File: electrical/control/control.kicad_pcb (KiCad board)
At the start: 2 copper layers, 33 x 48 mm, 42 parts, among them J1 USB4105-GF-A, J2 SWD, J3 TC2030-NL, J4 UART, J5 QWIIC, SW1 228EMSARGFR, U1 USBLC6-2P6, U2 LP5912-3.3DRV, U3 W25Q16JVUXIQ, U4 RP2040, U5 ABPMRRV060MG2A3, Y1 ABM8-272-T3

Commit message: More PCB tweaks
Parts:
- moved J5 2.41 mm to (166.5, 109.1)
- moved C18 2.41 mm to (161.0, 107.9)
- moved U5 2.41 mm to (154.0, 108.4)
- moved J3 2.15 mm to (166.4, 102.0)
- moved C10 2.00 mm to (153.4, 86.0)
- moved C11 2.00 mm to (155.0, 98.6)
- moved C12 2.00 mm to (152.4, 85.6)
- moved C13 2.00 mm to (157.6, 87.0)
- moved C14 2.00 mm to (156.6, 86.1)
- moved C15 2.00 mm to (147.6, 84.0)
- moved C16 2.00 mm to (152.0, 98.2)
- moved C17 2.00 mm to (152.0, 100.2)
- moved C4 2.00 mm to (148.6, 88.8)
- moved C5 2.00 mm to (148.6, 93.2)
- moved C6 2.00 mm to (154.0, 98.6)
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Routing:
- net RUN: track 26.7 -> 18.2 mm
- net I2C_SCL: track 38.4 -> 37.0 mm
- net SWDIO: track 20.7 -> 19.5 mm
- net Net-(U4-GPIO25): track 26.3 -> 25.2 mm
- net Net-(R8-Pad2): track 25.9 -> 24.7 mm
- net USB_D-: track 6.22 -> 7.37 mm
- net Net-(U4-GPIO26_ADC0): track 22.8 -> 21.6 mm
- net USB_D+: track 6.22 -> 7.37 mm
- net I2C_SDA: track 46.1 -> 45.2 mm
- net SWCLK: track 19.0 -> 18.2 mm
- net PRESSURE_INT: track 32.8 -> 32.0 mm
- net UART_TX: track 25.2 -> 24.6 mm
- net GND: track 62.5 -> 63.0 mm, vias 33 -> 32
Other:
- board size 33 x 48 mm -> 32 x 46 mm
- board text added: "BBMI MIDI Concertina Controller Rev 1"

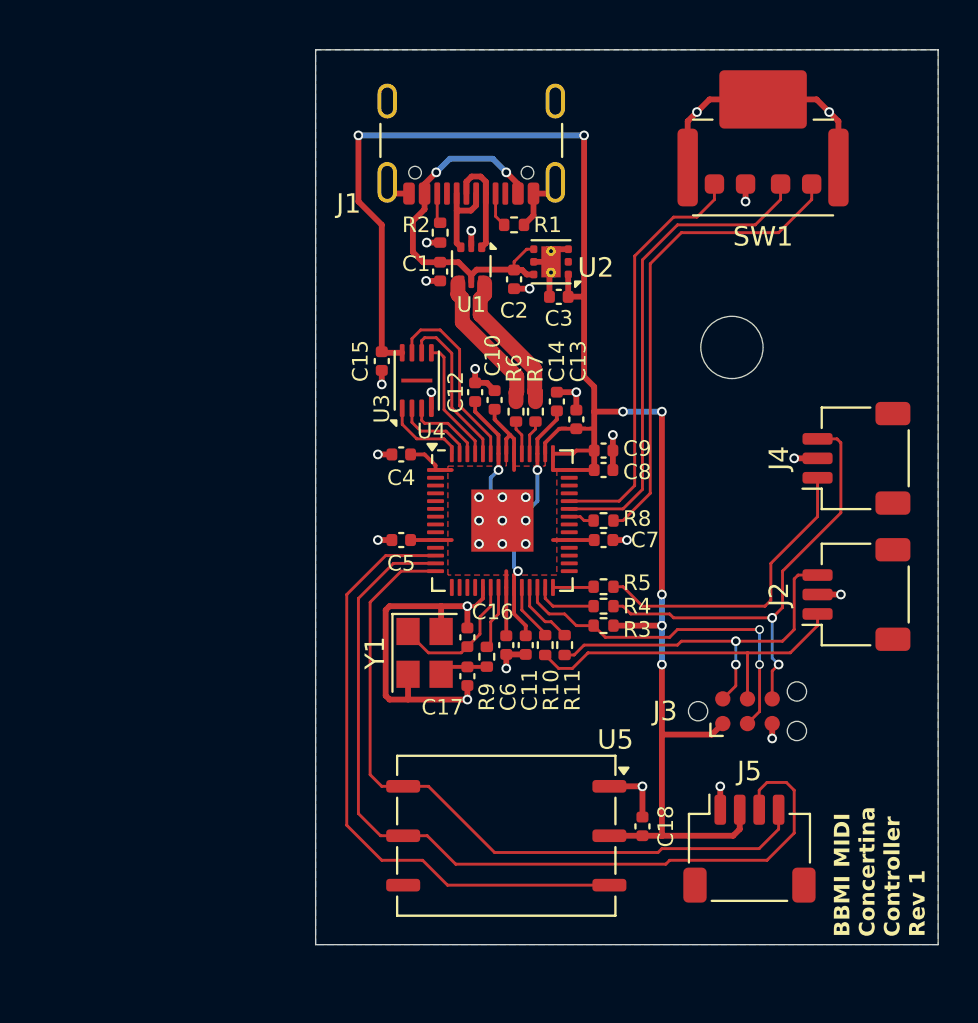
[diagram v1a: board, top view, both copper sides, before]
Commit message: Position mechanical components
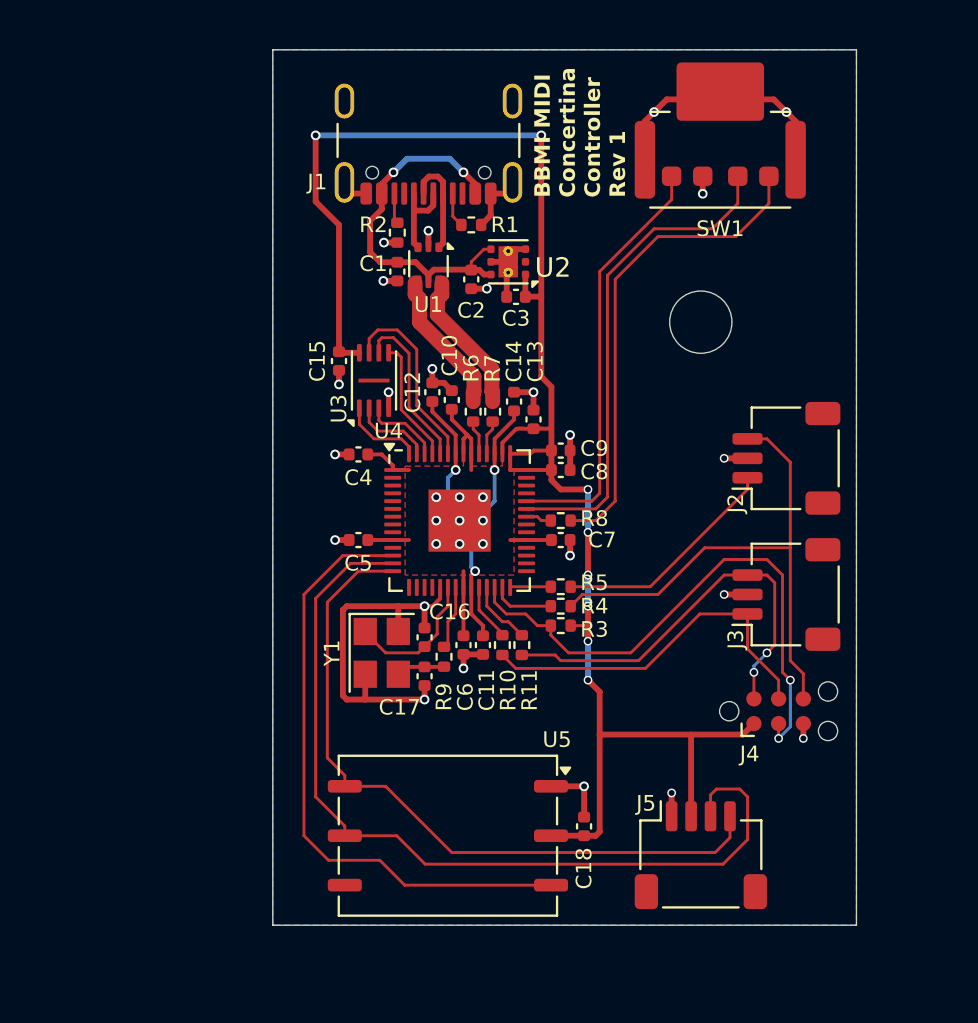
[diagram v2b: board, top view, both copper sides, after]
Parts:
- moved J2 3.60 mm to (168.4, 89.0)
- moved J3 3.60 mm to (168.4, 96.0)
- moved C18 3.00 mm to (158.0, 107.9)
- moved U5 3.00 mm to (151.0, 108.4)
- moved J5 2.52 mm to (164.0, 109.4)
- moved SW1 2.24 mm to (165.0, 74.5)
- moved C10 2.20 mm to (151.2, 86.0)
- moved C12 2.20 mm to (150.2, 85.6)
- moved C2 2.20 mm to (152.2, 79.8)
- moved R1 2.20 mm to (152.2, 77.0)
- moved U2 2.20 mm to (154.1, 78.9)
- moved U3 2.20 mm to (147.2, 85.0)
- moved U4 2.20 mm to (151.6, 92.2)
- moved Y1 2.20 mm to (147.6, 99.0)
- moved C1 2.20 mm to (148.4, 79.4)
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- renumbered J4 to J2, J2 to J3, J3 to J4
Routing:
- net RUN: track 18.2 -> 28.8 mm
- net UART_RX: track 15.9 -> 11.8 mm
- net UART_TX: track 24.6 -> 27.7 mm, vias 2 -> 0
- net +3.3V: track 105.9 -> 103.2 mm, vias 7 -> 8
- net SWDIO: track 19.5 -> 21.5 mm
- net SWCLK: track 18.2 -> 19.1 mm
- net I2C_SCL: track 37.0 -> 36.5 mm
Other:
- board size 32 x 46 mm -> 30 x 45 mm

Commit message: Replace illuminated button with separate components
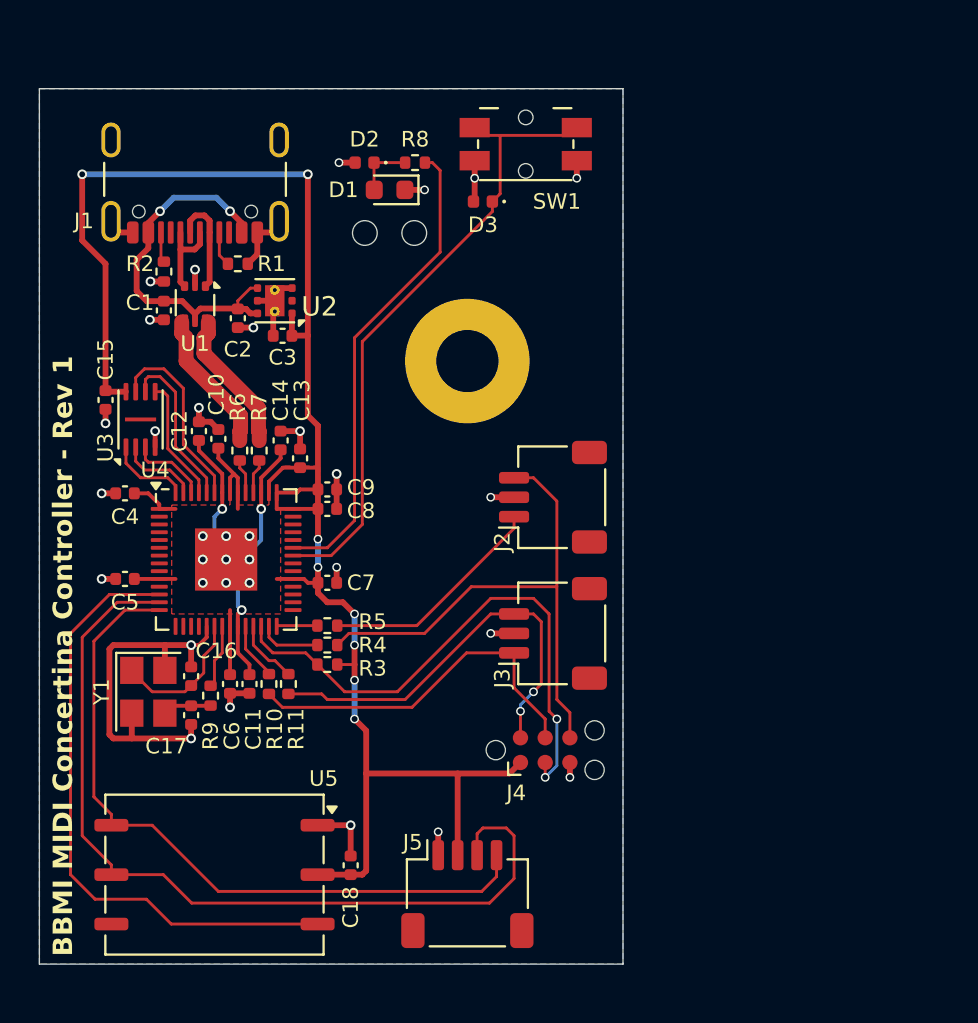
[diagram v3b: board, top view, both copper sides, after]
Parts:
- added D1: RED, LED_SMD:LED_0603_1608Metric, F.Cu at (148.0, 75.2)
- added D2: ESD351, Diode_SMD:D_0402_1005Metric, F.Cu at (146.7, 73.8)
- added D3: ESD351, Diode_SMD:D_0402_1005Metric, F.Cu at (152.8, 75.8)
- added LP1: ~, midi_concertina:SLP3-150-150-F, F.Cu at (148.0, 74.7)
- H1: footprint MountingHole:MountingHole_3.2mm_M3 -> MountingHole:MountingHole_3.2mm_M3_Pad
- SW1: value 228EMSARGFR -> SYS; footprint midi_concertina:CTS_228EMS -> Button_Switch_SMD:Panasonic_EVQPUL_EVQPUC
- moved R8 19.9 mm to (149.3, 73.8), turned to 180 degrees
- moved C7 12.2 mm to (144.8, 95.4)
- moved C1 12.2 mm to (136.4, 81.4)
- moved C10 12.2 mm to (139.2, 88.0)
- moved C11 12.2 mm to (140.8, 100.6)
- moved C12 12.2 mm to (138.2, 87.6)
- moved C13 12.2 mm to (143.4, 89.0)
- moved C14 12.2 mm to (142.4, 88.1)
- moved C15 12.2 mm to (133.4, 86.0)
- moved C16 12.2 mm to (137.8, 100.2)
- moved C17 12.2 mm to (137.8, 102.2)
- moved C18 12.2 mm to (146.0, 109.9)
- moved C2 12.2 mm to (140.2, 81.8)
- moved C3 12.2 mm to (142.5, 82.7)
- moved C4 12.2 mm to (134.4, 90.8)
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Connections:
- R8 pad 1: Net-(U4-GPIO24) -> Net-(U4-GPIO25)
- R8 pad 2: Net-(R8-Pad2) -> Net-(D1-A)
- U4 pad 36: Net-(U4-GPIO24) -> Net-(D3-K)
- U4 pad 38: Net-(U4-GPIO26_ADC0) -> unconnected-(U4-GPIO26_ADC0-Pad38)
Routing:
- net Net-(D3-K): track 0.00 -> 32.7 mm
- net Net-(R8-Pad2): track 25.0 -> 0.00 mm
- net Net-(U4-GPIO26_ADC0): track 21.8 -> 0.00 mm
- net GND: track 63.1 -> 53.6 mm, vias 32 -> 33
- net Net-(D1-A): track 0.00 -> 3.01 mm
- net Net-(U4-GPIO24): track 1.34 -> 0.00 mm
- net Net-(U4-GPIO25): track 25.4 -> 24.5 mm
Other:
- board text added: "BBMI MIDI Concertina Controller - Rev 1"
- board text removed: "BBMI MIDI Concertina Controller Rev 1"

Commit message: Label debug connectors
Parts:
- moved J4 0.40 mm to (155.6, 104.0)
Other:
- board text added: "SWD"
- board text added: "UART"
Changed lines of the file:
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@@
 		)
 		(embedded_fonts no)
-		(model "${KICAD9_3DMODEL_DIR}/Connector_JST.3dshapes/JST_SH_SM03B-SRSS-TB_1x03-1MP_P1.00mm_Horizontal.wrl"
+		(model "${KIPRJMOD}/../library/midi_concertina.3dshapes/JST_SH_SM03B-SRSS-TB_1x03-1MP_P1.00mm_Horizontal.wrl"
 			(offset
 				(xyz 0 0 0)
@@
 		)
 		(embedded_fonts no)
+		(model "${KIPRJMOD}/../library/midi_concertina.3dshapes/SLP3-150-150-F.IGS"
+			(offset
+				(xyz 2.25 3.85 0)
+			)
+			(scale
+				(xyz 1 1 1)
+			)
+			(rotate
+				(xyz -90 -0 90)
+			)
+		)
 	)
 	(footprint "Capacitor_SMD:C_0402_1005Metric"
@@
 		)
 		(embedded_fonts no)
-		(model "${KICAD9_3DMODEL_DIR}/Connector_JST.3dshapes/JST_SH_SM04B-SRSS-TB_1x04-1MP_P1.00mm_Horizontal.wrl"
+		(model "${KIPRJMOD}/../library/midi_concertina.3dshapes/JST_SH_SM04B-SRSS-TB_1x04-1MP_P1.00mm_Horizontal.wrl"
 			(offset
 				(xyz 0 0 0)
@@
 	(footprint "Connector:Tag-Connect_TC2030-IDC-NL_2x03_P1.27mm_Vertical"
 		(layer "F.Cu")
-		(at 156 104)
+		(at 155.6 104)
 		(descr "Tag-Connect programming header; http://www.tag-connect.com/Materials/TC2030-IDC-NL.pdf")
 		(tags "tag connect programming header pogo pins")
@@
 			(polygon
 				(pts
-					(xy 157.27 103.365) (xy 154.73 103.365) (xy 154.73 104.635) (xy 157.27 104.635)
+					(xy 156.87 103.365) (xy 154.33 103.365) (xy 154.33 104.635) (xy 156.87 104.635)
 				)
 			)
@@
 		)
 		(embedded_fonts no)
-		(model "${KICAD9_3DMODEL_DIR}/Connector_JST.3dshapes/JST_SH_SM03B-SRSS-TB_1x03-1MP_P1.00mm_Horizontal.wrl"
+		(model "${KIPRJMOD}/../library/midi_concertina.3dshapes/JST_SH_SM03B-SRSS-TB_1x03-1MP_P1.00mm_Horizontal.wrl"
 			(offset
 				(xyz 0 0 0)
@@
 			(at 0 3.5 0)
 			(layer "F.Fab")
+			(hide yes)
 			(effects
 				(font
@@
 		)
 		(embedded_fonts no)
-		(model "${KICAD9_3DMODEL_DIR}/Button_Switch_SMD.3dshapes/Panasonic_EVQPUL_EVQPUC.wrl"
+		(model "${KIPRJMOD}/../library/midi_concertina.3dshapes/Panasonic_EVQPUL_EVQPUC.wrl"
 			(offset
 				(xyz 0 0 0)
@@
 		(layer "User.2")
 	)
+	(gr_text "UART"
+		(at 152.8 91 90)
+		(layer "F.SilkS")
+		(effects
+			(font
+				(size 1 1)
+				(thickness 0.153)
+			)
+			(justify bottom)
+		)
+	)
+	(gr_text "SWD"
+		(at 152.8 98 90)
+		(layer "F.SilkS")
+		(effects
+			(font
+				(size 1 1)
+				(thickness 0.153)
+			)
+			(justify bottom)
+		)
+	)
 	(gr_text "BBMI MIDI Concertina Controller - Rev 1"
 		(at 131.8 114.6 90)
@@
 	)
 	(segment
-		(start 157.27 105.4)
-		(end 157.27 104.635)
-		(width 0.3)
-		(layer "F.Cu")
-		(net 2)
-	)
-	(segment
 		(start 141.2 77.39)
 		(end 142.12 77.39)
@@
 	)
 	(segment
+		(start 156.87 105.4)
+		(end 156.87 104.635)
+		(width 0.3)
+		(layer "F.Cu")
+		(net 2)
+	)
+	(segment
 		(start 148.7875 75.2)
 		(end 149.8 75.2)
@@
 	)
 	(via
-		(at 157.27 105.4)
+		(at 156.87 105.4)
 		(size 0.45)
 		(drill 0.3)
@@
 	)
 	(segment
-		(start 154.73 104.635)
-		(end 154.165 105.2)
-		(width 0.3)
-		(layer "F.Cu")
-		(net 3)
-	)
-	(segment
 		(start 143.8 82.69)
 		(end 142.99 82.69)
@@
 	)
 	(segment
-		(start 154.165 105.2)
-		(end 146.8 105.2)
+		(start 154.33 104.635)
+		(end 153.765 105.2)
 		(width 0.3)
 		(layer "F.Cu")
@@
 	)
 	(segment
+		(start 153.765 105.2)
+		(end 146.8 105.2)
+		(width 0.3)
+		(layer "F.Cu")
+		(net 3)
+	)
+	(segment
 		(start 143.2375 90.7625)
 		(end 143.4 90.6)
@@
 	)
 	(segment
-		(start 154.4 100.8)
+		(start 151.953405 99)
 		(end 154.4 99)
 		(width 0.15)
@@
 	)
 	(segment
-		(start 156 102.4)
-		(end 154.4 100.8)
+		(start 155.6 103.365)
+		(end 155.6 102)
 		(width 0.15)
 		(layer "F.Cu")
@@
 	)
 	(segment
-		(start 151.953405 99)
-		(end 154.4 99)
+		(start 142.49 101.8)
+		(end 149.153405 101.8)
 		(width 0.15)
 		(layer "F.Cu")
@@
 	)
 	(segment
-		(start 156 103.365)
-		(end 156 102.4)
+		(start 149.153405 101.8)
+		(end 151.953405 99)
 		(width 0.15)
 		(layer "F.Cu")
@@
 	)
 	(segment
-		(start 142.49 101.8)
-		(end 149.153405 101.8)
+		(start 141.8 101.11)
+		(end 142.49 101.8)
 		(width 0.15)
 		(layer "F.Cu")
@@
 	)
 	(segment
-		(start 149.153405 101.8)
-		(end 151.953405 99)
+		(start 155.6 102)
+		(end 154.4 100.8)
 		(width 0.15)
 		(layer "F.Cu")
@@
 	)
 	(segment
-		(start 141.8 101.11)
-		(end 142.49 101.8)
+		(start 154.4 100.8)
+		(end 154.4 99)
 		(width 0.15)
 		(layer "F.Cu")
@@
 	)
 	(segment
-		(start 154.73 102)
-		(end 154.73 103.365)
+		(start 154.33 102.07)
+		(end 154.33 103.365)
+		(width 0.15)
+		(layer "F.Cu")
+		(net 11)
+	)
+	(segment
+		(start 154.6 101.8)
+		(end 154.33 102.07)
 		(width 0.15)
 		(layer "F.Cu")
@@
 	)
 	(via
-		(at 154.73 102)
+		(at 154.6 101.8)
 		(size 0.45)
 		(drill 0.3)
@@
 	)
 	(segment
-		(start 154.73 102)
-		(end 154.73 101.67)
-		(width 0.15)
-		(layer "B.Cu")
-		(net 11)
-	)
-	(segment
-		(start 154.73 101.67)
+		(start 154.6 101.8)
 		(end 155.4 101)
 		(width 0.15)
@@
 	)
 	(segment
-		(start 157.27 103.365)
-		(end 157.27 102.07)
+		(start 145.31 98.6)
+		(end 145.91 98)
 		(width 0.15)
 		(layer "F.Cu")
@@
 	)
 	(segment
-		(start 156.6 91.2)
-		(end 155.4 90)
+		(start 156.87 103.365)
+		(end 156.87 101.67)
 		(width 0.15)
 		(layer "F.Cu")
@@
 	)
 	(segment
-		(start 145.31 98.6)
-		(end 145.91 98)
+		(start 156.6 91.2)
+		(end 155.4 90)
 		(width 0.15)
 		(layer "F.Cu")
@@
 	)
 	(segment
-		(start 157.27 102.07)
+		(start 156.87 101.67)
 		(end 156.6 101.4)
 		(width 0.15)
@@
 	)
 	(segment
-		(start 155.4 90)
-		(end 154.4 90)
+		(start 152.2 95.6)
+		(end 156.6 95.6)
 		(width 0.15)
 		(layer "F.Cu")
@@
 	)
 	(segment
-		(start 152.2 95.6)
-		(end 156.6 95.6)
+		(start 145.91 98)
+		(end 149.8 98)
 		(width 0.15)
 		(layer "F.Cu")
@@
 	)
 	(segment
-		(start 145.91 98)
-		(end 149.8 98)
+		(start 155.4 90)
+		(end 154.4 90)
 		(width 0.15)
 		(layer "F.Cu")
@@
 	)
 	(segment
-		(start 156 105.4)
-		(end 156 104.635)
+		(start 148.4 101)
+		(end 145.69 101)
 		(width 0.15)
 		(layer "F.Cu")
@@
 	)
 	(segment
-		(start 144.29 99.6)
-		(end 145.69 101)
+		(start 155.4 96.2)
+		(end 153.2 96.2)
 		(width 0.15)
 		(layer "F.Cu")
@@
 	)
 	(segment
-		(start 148.4 101)
-		(end 153.2 96.2)
+		(start 145.69 101)
+		(end 144.29 99.6)
 		(width 0.15)
 		(layer "F.Cu")
@@
 	)
 	(segment
-		(start 145.69 101)
-		(end 148.4 101)
-		(width 0.15)
-		(layer "F.Cu")
-		(net 14)
-	)
-	(segment
-		(start 156.2 102)
-		(end 156.6 102.4)
+		(start 156.2 97)
+		(end 155.4 96.2)
 		(width 0.15)
 		(layer "F.Cu")
@@
 	(segment
 		(start 153.2 96.2)
-		(end 155.4 96.2)
+		(end 148.4 101)
 		(width 0.15)
 		(layer "F.Cu")
@@
 	)
 	(segment
-		(start 155.4 96.2)
+		(start 156.2 102.4)
 		(end 156.2 97)
 		(width 0.15)
@@
 	)
 	(segment
-		(start 156.2 97)
-		(end 156.2 102)
+		(start 141.4 98.4)
+		(end 142 99)
 		(width 0.15)
 		(layer "F.Cu")
@@
 	)
 	(segment
-		(start 141.4 98.4)
-		(end 142 99)
+		(start 155.6 105.4)
+		(end 155.6 104.635)
 		(width 0.15)
 		(layer "F.Cu")
@@
 	)
 	(via
-		(at 156 105.4)
+		(at 155.6 105.4)
 		(size 0.45)
 		(drill 0.3)
@@
 	)
 	(via
-		(at 156.6 102.4)
+		(at 156.2 102.4)
 		(size 0.45)
 		(drill 0.3)
@@
 	)
 	(segment
-		(start 156.6 102.4)
-		(end 156.6 104.8)
+		(start 156.2 104.8)
+		(end 155.6 105.4)
 		(width 0.15)
 		(layer "B.Cu")
@@
 	)
 	(segment
-		(start 156.6 104.8)
-		(end 156 105.4)
+		(start 156.2 102.4)
+		(end 156.2 104.8)
 		(width 0.15)
 		(layer "B.Cu")

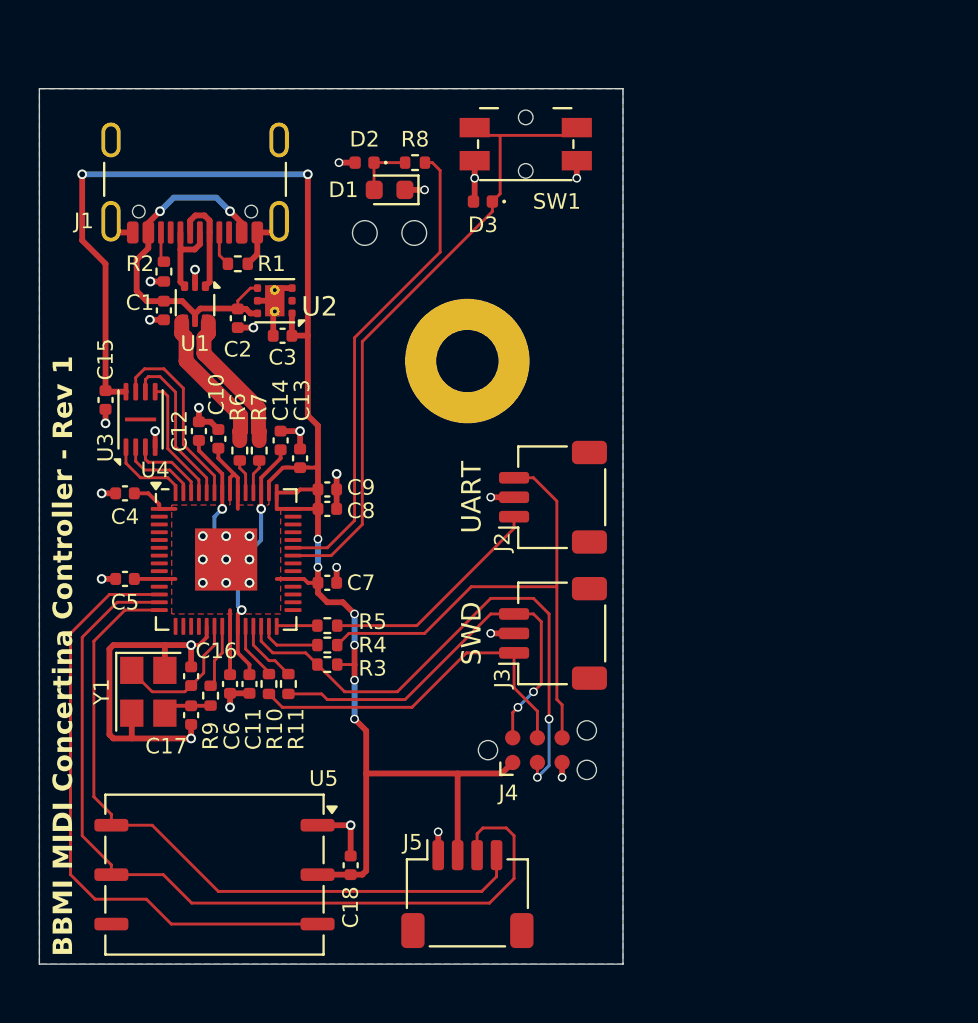
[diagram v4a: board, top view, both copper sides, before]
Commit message: Update parts for controller board
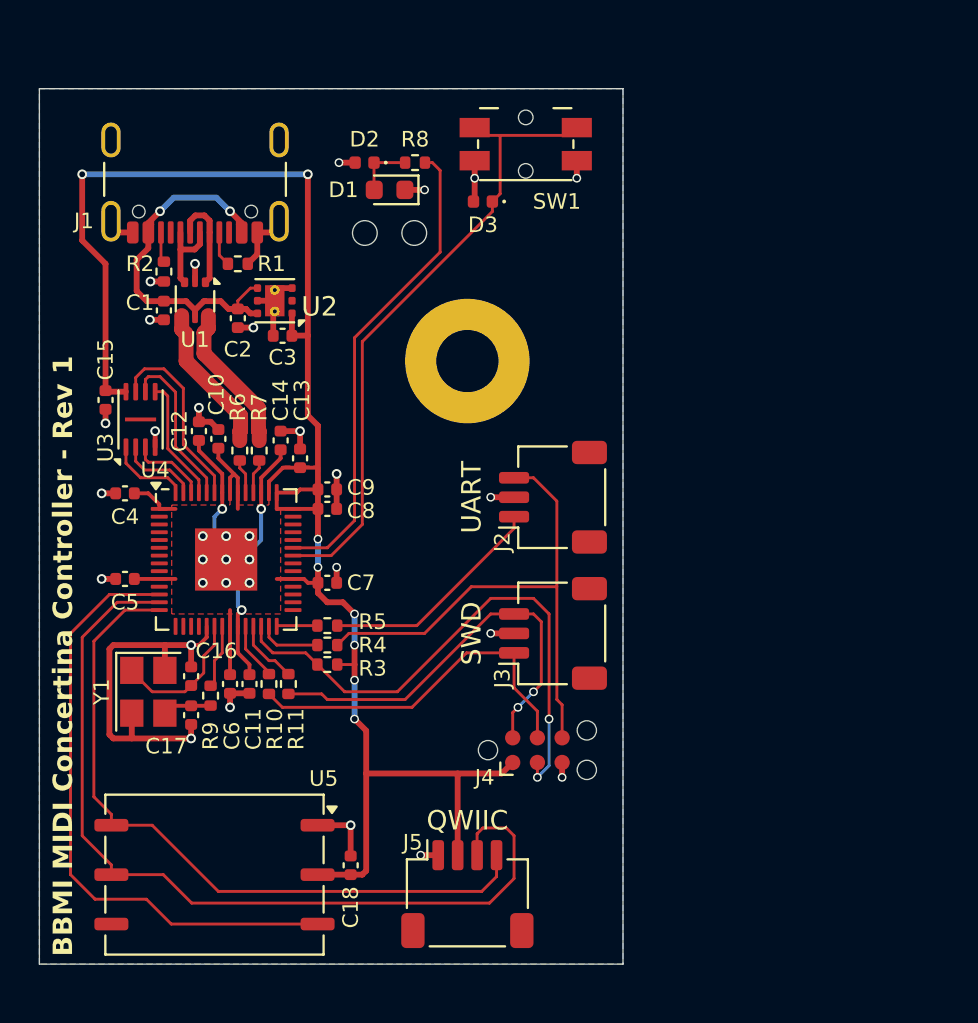
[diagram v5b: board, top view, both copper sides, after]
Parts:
- LP1: value ~ -> SLP-150-150-F
- moved U1 0.20 mm to (138.0, 80.8)
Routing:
- net VBUS: track 19.1 -> 21.4 mm
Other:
- board text added: "QWIIC"
